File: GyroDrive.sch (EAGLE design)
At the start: 55 parts, among them IC1 AD8235, IC2 AD8235, IC3 AD8235, IC4 AD8235

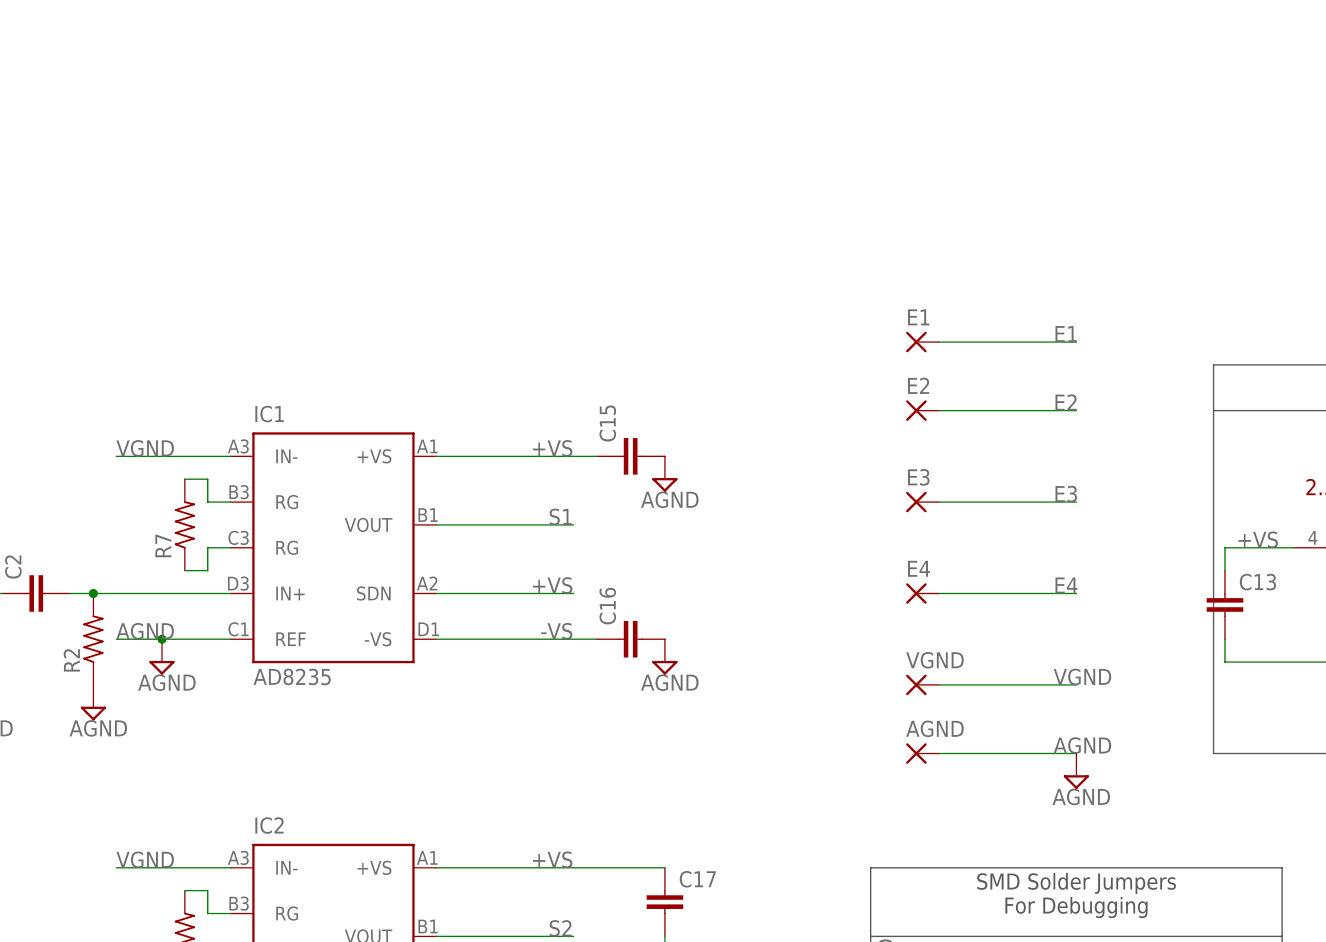
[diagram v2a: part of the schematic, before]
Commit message: Added high pass filter for VGND. Attachment point for AGND changed to through hole.
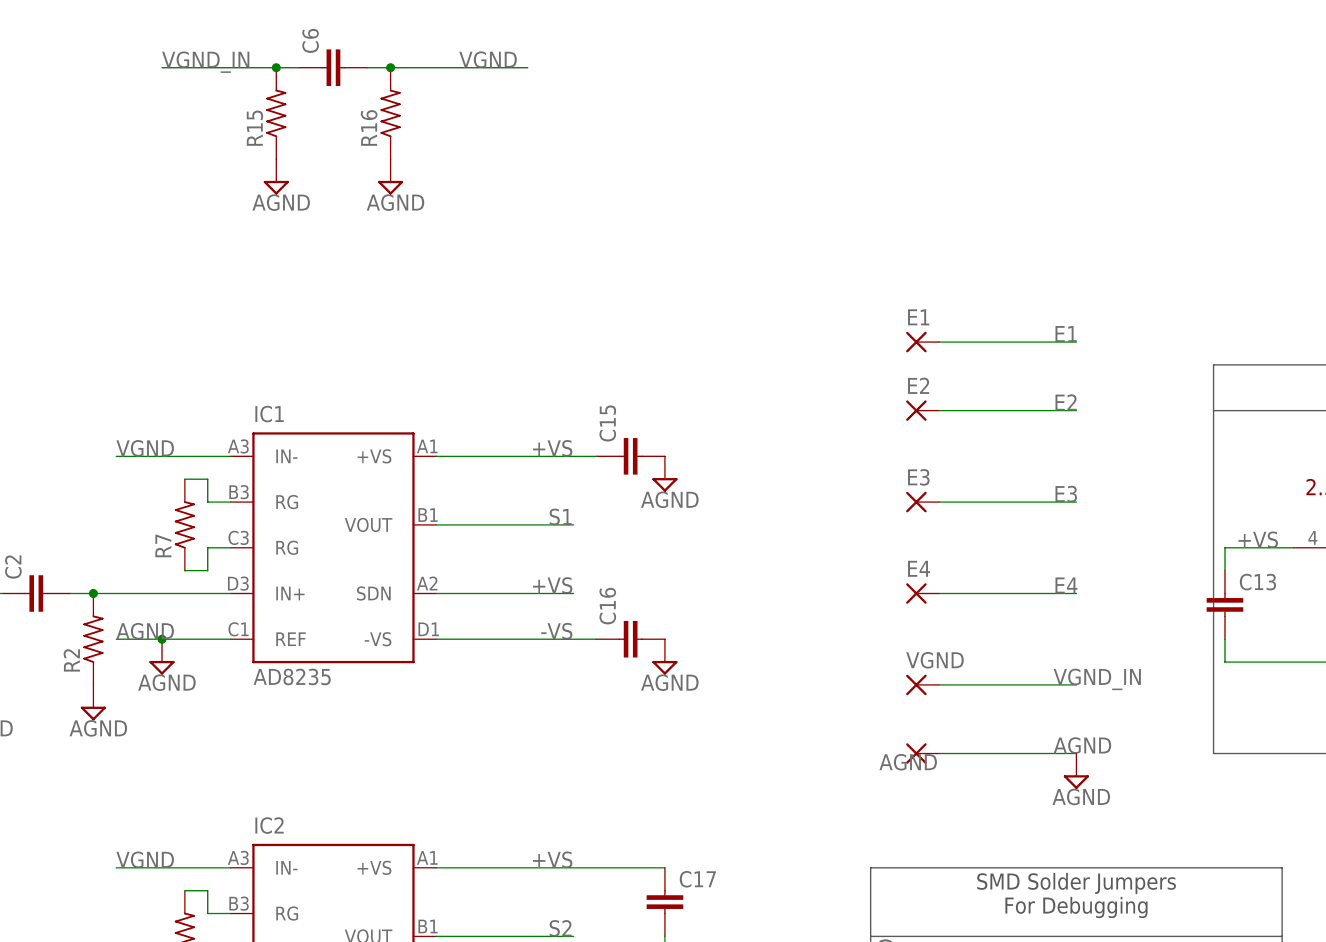
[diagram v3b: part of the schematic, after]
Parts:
- added C6: (no value), resistor:C-EUC0201
- added R15, R16: (no value), resistor:R-US_R0201
- AGND: device michael-stetner:SMD25-25-MIL -> michael-stetner:THROUGH-HOLE-30MIL/15MIL
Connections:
- new net VGND_IN: C6.1, R15.2, VGND.P
- net AGND: now also R15.1, R16.1
- net VGND: now also C6.2, R16.2; no longer VGND.P
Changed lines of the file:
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@@
 <part name="E4" library="michael-stetner" deviceset="SMD25-25-MIL" device=""/>
 <part name="VGND" library="michael-stetner" deviceset="SMD25-25-MIL" device=""/>
-<part name="AGND" library="michael-stetner" deviceset="SMD25-25-MIL" device=""/>
 <part name="E1" library="michael-stetner" deviceset="SMD25-25-MIL" device=""/>
 <part name="C1" library="resistor" deviceset="C-EU" device="C0201"/>
@@
 <part name="SUPPLY10" library="supply2" deviceset="AGND" device=""/>
 <part name="SUPPLY11" library="supply2" deviceset="AGND" device=""/>
+<part name="R15" library="resistor" deviceset="R-US_" device="R0201"/>
+<part name="C6" library="resistor" deviceset="C-EU" device="C0201"/>
+<part name="R16" library="resistor" deviceset="R-US_" device="R0201"/>
+<part name="SUPPLY30" library="supply2" deviceset="AGND" device=""/>
+<part name="SUPPLY31" library="supply2" deviceset="AGND" device=""/>
+<part name="AGND" library="michael-stetner" deviceset="THROUGH-HOLE-30MIL/15MIL" device=""/>
 </parts>
 <sheets>
@@
 <instance part="E4" gate="1" x="96.52" y="149.86"/>
 <instance part="VGND" gate="1" x="96.52" y="139.7"/>
-<instance part="AGND" gate="1" x="96.52" y="132.08"/>
 <instance part="E1" gate="1" x="96.52" y="177.8"/>
 <instance part="C1" gate="G$1" x="104.14" y="106.68" rot="R90"/>
@@
 <instance part="SUPPLY10" gate="G$1" x="-7.62" y="10.16"/>
 <instance part="SUPPLY11" gate="G$1" x="5.08" y="10.16"/>
+<instance part="R15" gate="G$1" x="25.4" y="203.2" rot="R90"/>
+<instance part="C6" gate="G$1" x="30.48" y="208.28" rot="R90"/>
+<instance part="R16" gate="G$1" x="38.1" y="203.2" rot="R90"/>
+<instance part="SUPPLY30" gate="G$1" x="25.4" y="195.58"/>
+<instance part="SUPPLY31" gate="G$1" x="38.1" y="195.58"/>
+<instance part="AGND" gate="P" x="96.52" y="132.08" smashed="yes">
+<attribute name="NAME" x="98.933" y="132.0038" size="1.778" layer="95" rot="R180"/>
+<attribute name="VALUE" x="95.377" y="128.778" size="1.778" layer="96"/>
+</instance>
 </instances>
 <busses>
@@
 <label x="111.76" y="132.08" size="1.778" layer="95"/>
 <pinref part="SUPPLY1" gate="G$1" pin="AGND"/>
-<pinref part="AGND" gate="1" pin="P"/>
+<pinref part="AGND" gate="P" pin="P"/>
 </segment>
 <segment>
@@
 <pinref part="SUPPLY11" gate="G$1" pin="AGND"/>
 </segment>
+<segment>
+<pinref part="R15" gate="G$1" pin="1"/>
+<pinref part="SUPPLY30" gate="G$1" pin="AGND"/>
+</segment>
+<segment>
+<pinref part="R16" gate="G$1" pin="1"/>
+<pinref part="SUPPLY31" gate="G$1" pin="AGND"/>
+</segment>
 </net>
 <net name="S1" class="0">
@@
 </segment>
 <segment>
-<wire x1="99.06" y1="139.7" x2="114.3" y2="139.7" width="0.1524" layer="91"/>
-<label x="111.76" y="139.7" size="1.778" layer="95"/>
-<pinref part="VGND" gate="1" pin="P"/>
-</segment>
-<segment>
 <pinref part="J_VGND" gate="1" pin="1"/>
 <wire x1="111.76" y1="63.5" x2="96.52" y2="63.5" width="0.1524" layer="91"/>
 <label x="96.52" y="63.5" size="1.778" layer="95"/>
+</segment>
+<segment>
+<pinref part="R16" gate="G$1" pin="2"/>
+<wire x1="53.34" y1="208.28" x2="38.1" y2="208.28" width="0.1524" layer="91"/>
+<pinref part="C6" gate="G$1" pin="2"/>
+<wire x1="35.56" y1="208.28" x2="38.1" y2="208.28" width="0.1524" layer="91"/>
+<junction x="38.1" y="208.28"/>
+<label x="45.72" y="208.28" size="1.778" layer="95"/>
 </segment>
 </net>
@@
 </segment>
 </net>
+<net name="VGND_IN" class="0">
+<segment>
+<wire x1="99.06" y1="139.7" x2="114.3" y2="139.7" width="0.1524" layer="91"/>
+<label x="111.76" y="139.7" size="1.778" layer="95"/>
+<pinref part="VGND" gate="1" pin="P"/>
+</segment>
+<segment>
+<pinref part="C6" gate="G$1" pin="1"/>
+<pinref part="R15" gate="G$1" pin="2"/>
+<wire x1="27.94" y1="208.28" x2="25.4" y2="208.28" width="0.1524" layer="91"/>
+<wire x1="25.4" y1="208.28" x2="12.7" y2="208.28" width="0.1524" layer="91"/>
+<junction x="25.4" y="208.28"/>
+<label x="12.7" y="208.28" size="1.778" layer="95"/>
+</segment>
+</net>

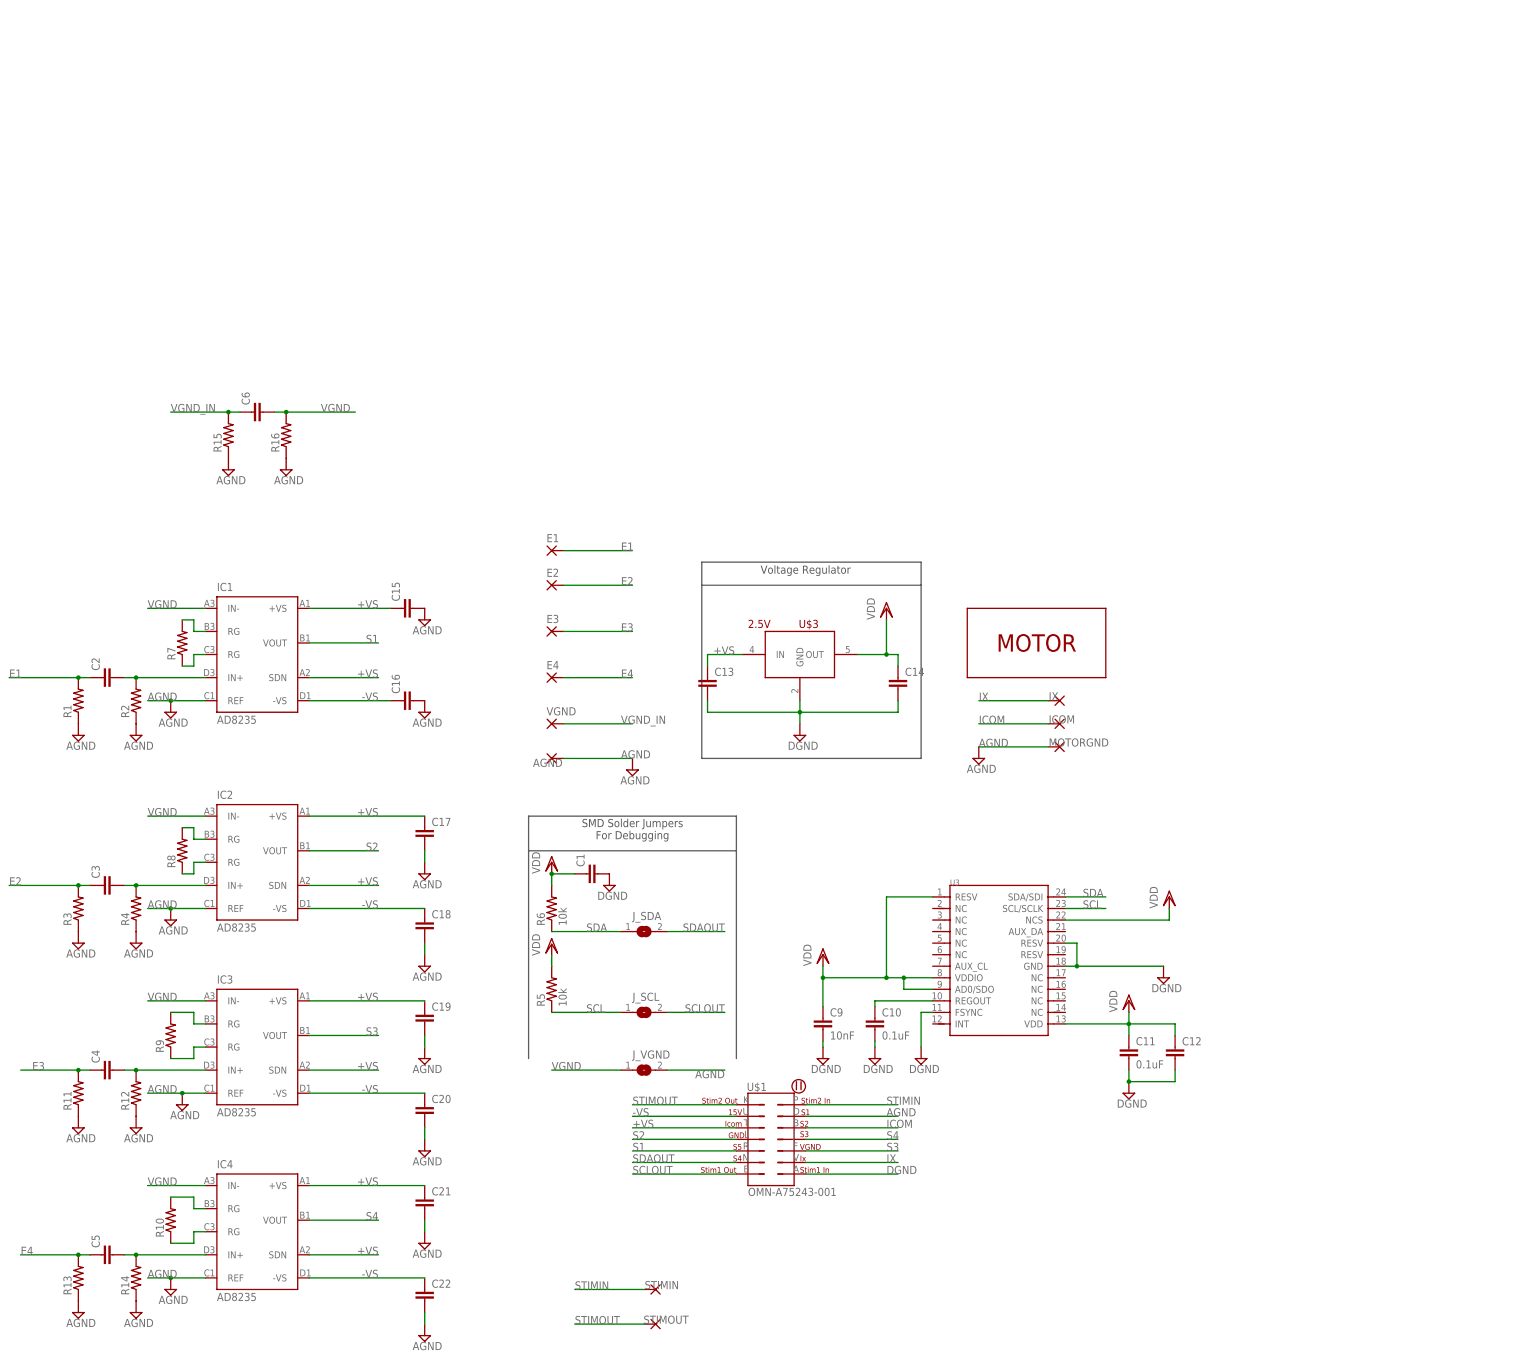
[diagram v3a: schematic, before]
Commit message: New instrumentation amplifier - AD8224. Old amplifier had too low bandwidth.
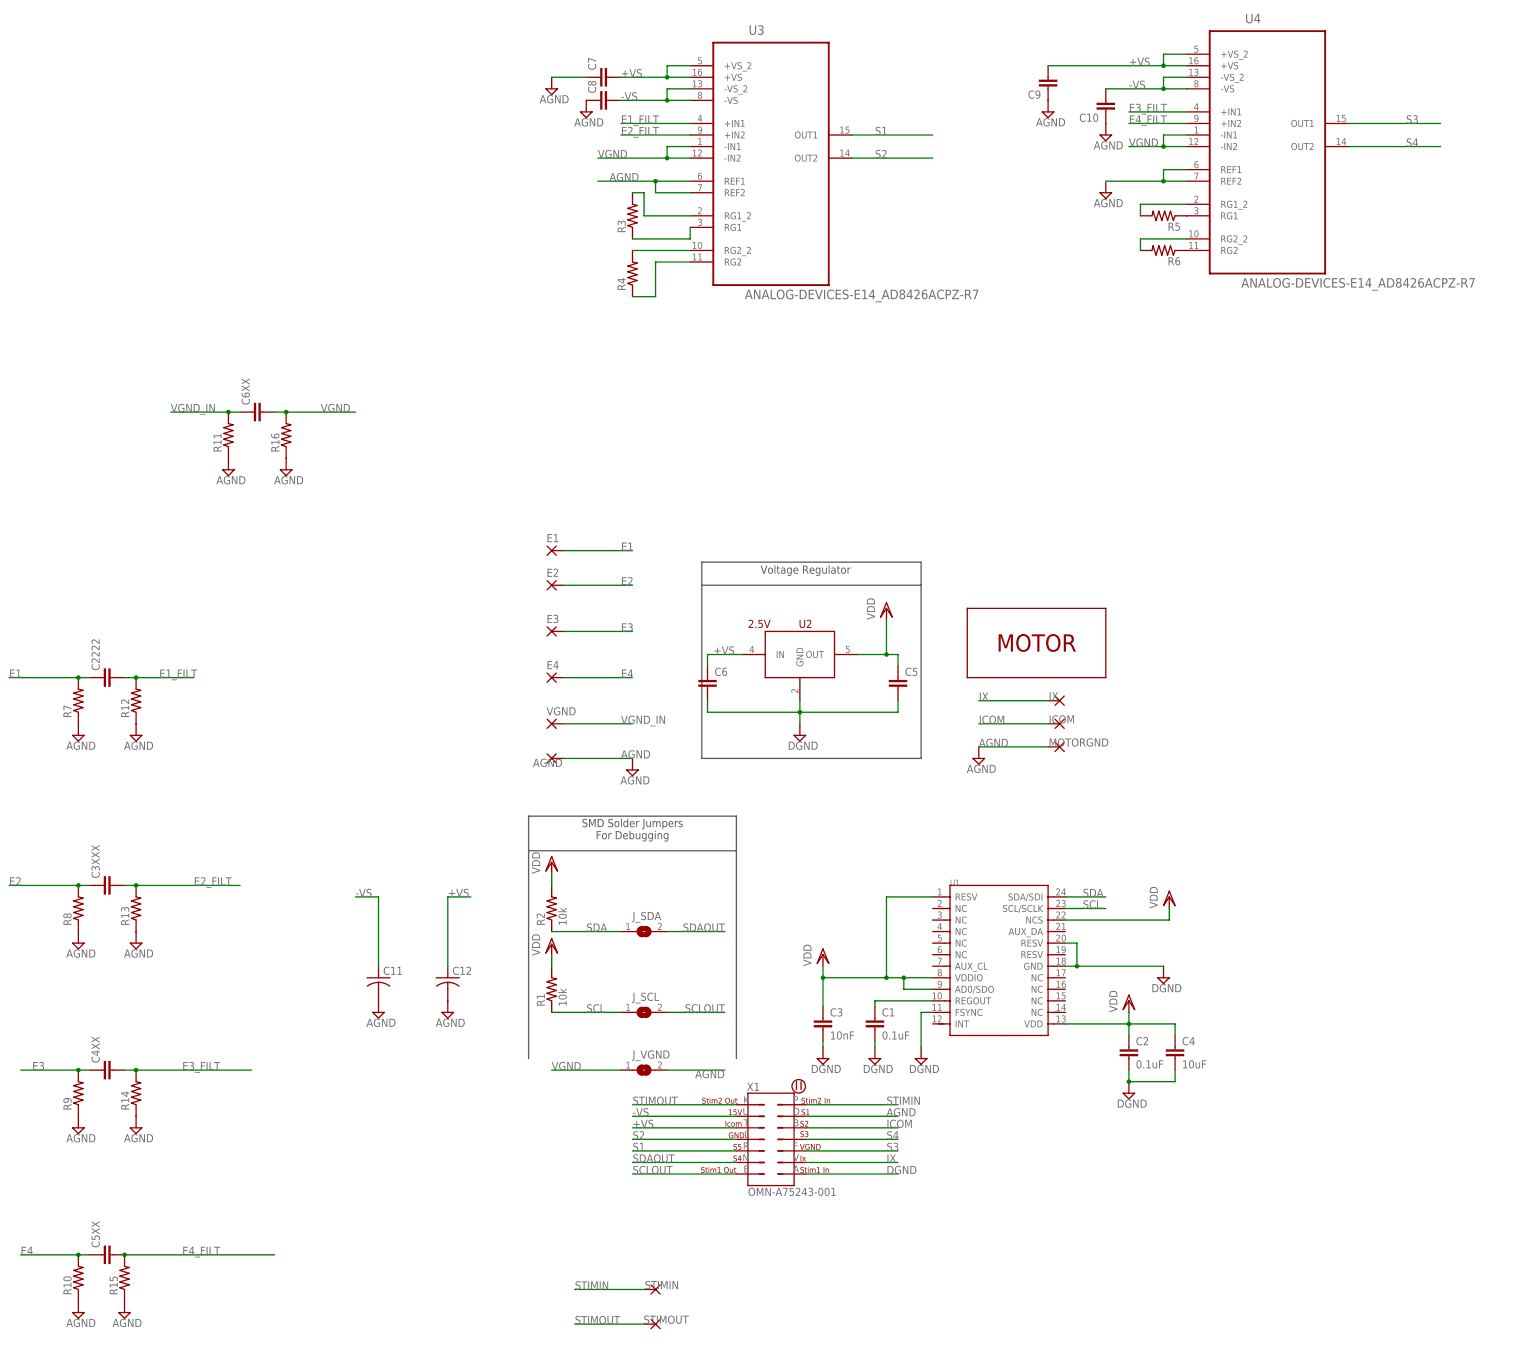
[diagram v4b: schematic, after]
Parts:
- removed C13, C14: (no value), resistor:C-EUC0402
- removed C15, C16, C17, C18, C19, C20, C21, C22: (no value), resistor:C-EUC0201
- removed IC1, IC2, IC3, IC4: AD8235, analog-devices:AD8235
- added C2222, C3XXX, C4XX, C5XX, C6XX, C7, C8: (no value), resistor:C-EUC0201
- added U1: (no value), Grove - IMU 10DOF v1.1:MPU-9250
- added U4: ANALOG-DEVICES-E14_AD8426ACPZ-R7, AD8426x2 wide:ANALOG-DEVICES-E14_AD8426ACPZ-R7
- C1, C2: value (none) -> 0.1uF; device resistor:C-EUC0201 -> resistor:C-EUC0402
- C10: value 0.1uF -> (none); device resistor:C-EUC0402 -> resistor:C-EUC0201
- C11: value 0.1uF -> (none); device resistor:C-EUC0402 -> resistor:C-USC0603
- C12: device resistor:C-EUC0603 -> resistor:C-USC0603
- C3: value (none) -> 10nF; device resistor:C-EUC0201 -> resistor:C-EUC0402
- C4: value (none) -> 10uF; device resistor:C-EUC0201 -> resistor:C-EUC0603
- C5, C6: device resistor:C-EUC0201 -> resistor:C-EUC0402
- C9: value 10nF -> (none); device resistor:C-EUC0402 -> resistor:C-EUC0201
- R1, R2: value (none) -> 10k
- R5, R6: value 10k -> (none)
- U3: value (none) -> ANALOG-DEVICES-E14_AD8426ACPZ-R7; device Grove - IMU 10DOF v1.1:MPU-9250 -> AD8426x2 wide:ANALOG-DEVICES-E14_AD8426ACPZ-R7
- renumbered U$1 to X1, U$3 to U2
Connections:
- removed net N$18: IC1.RG@1, R7.1
- removed net N$19: IC1.RG@2, R7.2
- removed net N$20: IC2.RG@2, R8.2
- removed net N$21: IC2.RG@1, R8.1
- removed net N$22: IC3.RG@2, R9.2
- removed net N$23: IC3.RG@1, R9.1
- removed net N$24: IC4.RG@2, R10.2
- removed net N$25: IC4.RG@1, R10.1
- removed net N$4: C4.2, IC3.IN+, R12.2
- removed net N$6: C2.2, IC1.IN+, R2.2
- removed net N$8: C5.2, IC4.IN+, R14.2
- removed net N$9: C3.2, IC2.IN+, R4.2
- new net E1_FILT: C2222.2, R12.2, U3.+IN1
- new net E2_FILT: C3XXX.2, R13.2, U3.+IN2
- new net E3_FILT: C4XX.2, R14.2, U4.+IN1
- new net E4_FILT: C5XX.2, R15.2, U4.+IN2
- new net N$10: R4.1, U3.RG2
- new net N$11: R3.1, U3.RG1
- new net N$12: R3.2, U3.RG1_2
- new net N$14: R5.1, U4.RG1
- new net N$15: R5.2, U4.RG1_2
- new net N$16: R6.2, U4.RG2_2
- new net N$17: R6.1, U4.RG2
- new net N$5: R4.2, U3.RG2_2
- net +VS: now also C12.1, C6.1, C7.2, C9.2, U3.+VS, U3.+VS_2, U4.+VS, U4.+VS_2; no longer C13.1, C15.1, C17.1, C19.1, C21.1, IC1.+VS, IC1.SDN, IC2.+VS, IC2.SDN, IC3.+VS, IC3.SDN, IC4.+VS, IC4.SDN
- net -VS: now also C10.2, C11.1, C8.2, U3.-VS, U3.-VS_2, U4.-VS, U4.-VS_2; no longer C16.1, C18.1, C20.1, C22.1, IC1.-VS, IC2.-VS, IC3.-VS, IC4.-VS
- net AGND: now also C10.1, C11.2, C12.2, C7.1, C8.1, C9.1, R10.1, R7.1, R8.1, R9.1, U3.REF1, U3.REF2, U4.REF1, U4.REF2; no longer C15.2, C16.2, C17.2, C18.2, C19.2, C20.2, C21.2, C22.2, IC1.REF, IC2.REF, IC3.REF, IC4.REF, R1.1, R2.1, R3.1, R4.1
- net DGND: now also C2.2, C3.2, C4.2, C5.2, C6.2, U1.FSYNC, U1.GND, U1.RESV@2; no longer C10.2, C11.2, C12.2, C13.2, C14.2, C9.2, U3.FSYNC, U3.GND, U3.RESV@2
- net E1: now also C2222.1, R7.2; no longer C2.1, R1.2
- net E2: now also C3XXX.1, R8.2; no longer C3.1, R3.2
- net E3: now also C4XX.1, R9.2; no longer C4.1, R11.2
- net E4: now also C5XX.1, R10.2; no longer C5.1, R13.2
- net N$7: now also C1.1, U1.REGOUT; no longer C10.1, U3.REGOUT
- net S1: now also U3.OUT1; no longer IC1.VOUT
- net S2: now also U3.OUT2; no longer IC2.VOUT
- net S3: now also U4.OUT1; no longer IC3.VOUT
- net S4: now also U4.OUT2; no longer IC4.VOUT
- net SCL: now also R1.1, U1.SCL/SCLK; no longer R5.1, U3.SCL/SCLK
- net SDA: now also R2.1, U1.SDA/SDI; no longer R6.1, U3.SDA/SDI
- net VDD: now also C2.1, C3.1, C4.1, C5.1, R1.2, R2.2, U1.AD0/SDO, U1.NCS, U1.RESV, U1.VDD, U1.VDDIO; no longer C1.1, C11.1, C12.1, C14.1, C9.1, R5.2, R6.2, U3.AD0/SDO, U3.NCS, U3.RESV, U3.VDD, U3.VDDIO
- net VGND: now also C6XX.2, U3.-IN1, U3.-IN2, U4.-IN1, U4.-IN2; no longer C6.2, IC1.IN-, IC2.IN-, IC3.IN-, IC4.IN-
- net VGND_IN: now also C6XX.1, R11.2; no longer C6.1, R15.2
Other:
- moved on the sheet: C1, C10, C11, C12, C2, C3, C4, C5, C6, C9, R1, R10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
